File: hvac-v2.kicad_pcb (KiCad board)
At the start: 2 copper layers, 114 x 60 mm, 35 parts, among them J2 Anderson_two_redblack, J3 Anderson_two_redblack, J4 Anderson_two_redblack, P1 10118194, P2 CONN_01X08, SW1 SW_SPST, SW3 KS-01Q-01, SW4 KS-01Q-01, SW5 SPST, U1 SAMD21E18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

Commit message: Add silkscreen version and test/cal
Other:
- board text added: "CAL"
- board text added: "HVAC v2.0 By: CandyKingdom GDPR compliant"
- board text added: "TEST"
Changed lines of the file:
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@@
     (links 90)
     (no_connects 0)
-    (area 45.924999 44.924999 160.075001 104.075001)
+    (area 45.924999 43.924999 160.075001 104.075001)
     (thickness 1.6)
-    (drawings 4)
+    (drawings 59)
     (tracks 477)
     (zones 0)
@@
       (net 4 FAN_OUT))
   )
+  (gr_line (start 127.4 101.6) (end 127.8 101.6) (layer F.SilkS) (width 0.2))
+  (gr_line (start 127.8 101.6) (end 127.8 101.5) (layer F.SilkS) (width 0.2))
+  (gr_line (start 127.9 101.7) (end 127.9 101.4) (layer F.SilkS) (width 0.2))
+  (gr_line (start 127.9 101.4) (end 127.4 101.4) (layer F.SilkS) (width 0.2))
+  (gr_line (start 127.8 101.5) (end 127.5 101.5) (layer F.SilkS) (width 0.2))
+  (gr_line (start 127.4 101.4) (end 127.4 101.6) (layer F.SilkS) (width 0.2))
+  (gr_line (start 128 101.8) (end 128 101.3) (layer F.SilkS) (width 0.2))
+  (gr_line (start 127.2 101.7) (end 127.9 101.7) (layer F.SilkS) (width 0.2))
+  (gr_line (start 127.2 101.3) (end 127.2 101.7) (layer F.SilkS) (width 0.2))
+  (gr_line (start 127.1 101.2) (end 127.1 101.8) (layer F.SilkS) (width 0.2))
+  (gr_line (start 128 101.3) (end 127.2 101.3) (layer F.SilkS) (width 0.2))
+  (gr_line (start 128.1 101.2) (end 127.1 101.2) (layer F.SilkS) (width 0.2))
+  (gr_line (start 127.1 101.8) (end 128 101.8) (layer F.SilkS) (width 0.2))
+  (gr_line (start 128.4 100.8) (end 126.8 100.8) (layer F.SilkS) (width 0.2))
+  (gr_line (start 127 101.1) (end 127 101.9) (layer F.SilkS) (width 0.2))
+  (gr_line (start 126.9 101) (end 126.9 102) (layer F.SilkS) (width 0.2))
+  (gr_line (start 126.8 102.1) (end 128.4 102.1) (layer F.SilkS) (width 0.2))
+  (gr_line (start 126.8 100.8) (end 126.8 102.1) (layer F.SilkS) (width 0.2))
+  (gr_line (start 126.9 102) (end 128.2 102) (layer F.SilkS) (width 0.2))
+  (gr_line (start 128.2 102) (end 128.2 101.1) (layer F.SilkS) (width 0.2))
+  (gr_line (start 128.1 101.9) (end 128.1 101.2) (layer F.SilkS) (width 0.2))
+  (gr_line (start 127 101.9) (end 128.1 101.9) (layer F.SilkS) (width 0.2))
+  (gr_line (start 128.4 102.1) (end 128.4 101) (layer F.SilkS) (width 0.2))
+  (gr_line (start 128.4 100.8) (end 128.4 101) (layer F.SilkS) (width 0.2))
+  (gr_line (start 128.2 101.1) (end 127 101.1) (layer F.SilkS) (width 0.2))
+  (gr_line (start 128.4 101) (end 126.9 101) (layer F.SilkS) (width 0.2))
+  (gr_line (start 127.4 98.8) (end 127.4 99) (layer F.SilkS) (width 0.2))
+  (gr_line (start 127.2 98.7) (end 127.2 99.1) (layer F.SilkS) (width 0.2))
+  (gr_line (start 128 98.7) (end 127.2 98.7) (layer F.SilkS) (width 0.2))
+  (gr_line (start 128.1 98.6) (end 127.1 98.6) (layer F.SilkS) (width 0.2))
+  (gr_line (start 127.8 98.9) (end 127.5 98.9) (layer F.SilkS) (width 0.2))
+  (gr_line (start 127.8 99) (end 127.8 98.9) (layer F.SilkS) (width 0.2))
+  (gr_line (start 127.4 99) (end 127.8 99) (layer F.SilkS) (width 0.2))
+  (gr_line (start 127.9 98.8) (end 127.4 98.8) (layer F.SilkS) (width 0.2))
+  (gr_line (start 127.9 99.1) (end 127.9 98.8) (layer F.SilkS) (width 0.2))
+  (gr_line (start 127.2 99.1) (end 127.9 99.1) (layer F.SilkS) (width 0.2))
+  (gr_line (start 127.1 99.2) (end 128 99.2) (layer F.SilkS) (width 0.2))
+  (gr_line (start 127.1 98.6) (end 127.1 99.2) (layer F.SilkS) (width 0.2))
+  (gr_line (start 128 99.2) (end 128 98.7) (layer F.SilkS) (width 0.2))
+  (gr_line (start 128.1 99.3) (end 128.1 98.6) (layer F.SilkS) (width 0.2))
+  (gr_line (start 128.2 98.5) (end 127 98.5) (layer F.SilkS) (width 0.2))
+  (gr_line (start 127 99.3) (end 128.1 99.3) (layer F.SilkS) (width 0.2))
+  (gr_line (start 128.4 98.4) (end 126.9 98.4) (layer F.SilkS) (width 0.2))
+  (gr_line (start 126.9 99.4) (end 128.2 99.4) (layer F.SilkS) (width 0.2))
+  (gr_line (start 128.4 99.5) (end 128.4 98.4) (layer F.SilkS) (width 0.2))
+  (gr_line (start 128.4 98.2) (end 128.4 98.4) (layer F.SilkS) (width 0.2))
+  (gr_line (start 128.2 99.4) (end 128.2 98.5) (layer F.SilkS) (width 0.2))
+  (gr_line (start 127 98.5) (end 127 99.3) (layer F.SilkS) (width 0.2))
+  (gr_line (start 126.9 98.4) (end 126.9 99.4) (layer F.SilkS) (width 0.2))
+  (gr_line (start 126.8 99.5) (end 128.4 99.5) (layer F.SilkS) (width 0.2))
+  (gr_line (start 126.8 98.2) (end 126.8 99.5) (layer F.SilkS) (width 0.2))
+  (gr_line (start 128.4 98.2) (end 126.8 98.2) (layer F.SilkS) (width 0.2))
+  (gr_text CAL (at 131 98.9) (layer F.SilkS)
+    (effects (font (size 1.5 1.5) (thickness 0.3)))
+  )
+  (gr_text TEST (at 131.6 101.5) (layer F.SilkS)
+    (effects (font (size 1.5 1.5) (thickness 0.3)))
+  )
+  (gr_text "HVAC v2.0\nBy: CandyKingdom\nGDPR compliant" (at 107.7 95.2) (layer F.SilkS)
+    (effects (font (size 1.5 1.5) (thickness 0.3)))
+  )
   (gr_line (start 46 104) (end 46 44) (layer Edge.Cuts) (width 0.15))

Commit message: Place the programming header and diode
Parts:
- added D1: BAT54GWJ, Diodes_SMD:SOD-123, F.Cu at (60.3, 83.6)
- added J1: Conn_01x04, Pin_Headers:Pin_Header_Straight_1x04, F.Cu at (112.1, 101.8)
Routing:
- net ARM_SWCLK: track 0.00 -> 27.2 mm, vias 0 -> 2
- net ARM_SWDIO: track 0.00 -> 24.9 mm, vias 0 -> 2
- net VCC: track 391.0 -> 405.2 mm, vias 15 -> 16
- net Net-(D1-Pad2): track 0.00 -> 10.2 mm
- net +BATT: track 183.2 -> 190.2 mm
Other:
- board text added: "FAN"
- board text added: "GND CLK IO VCC"
- board text added: "IN"
- board text added: "PUMP"

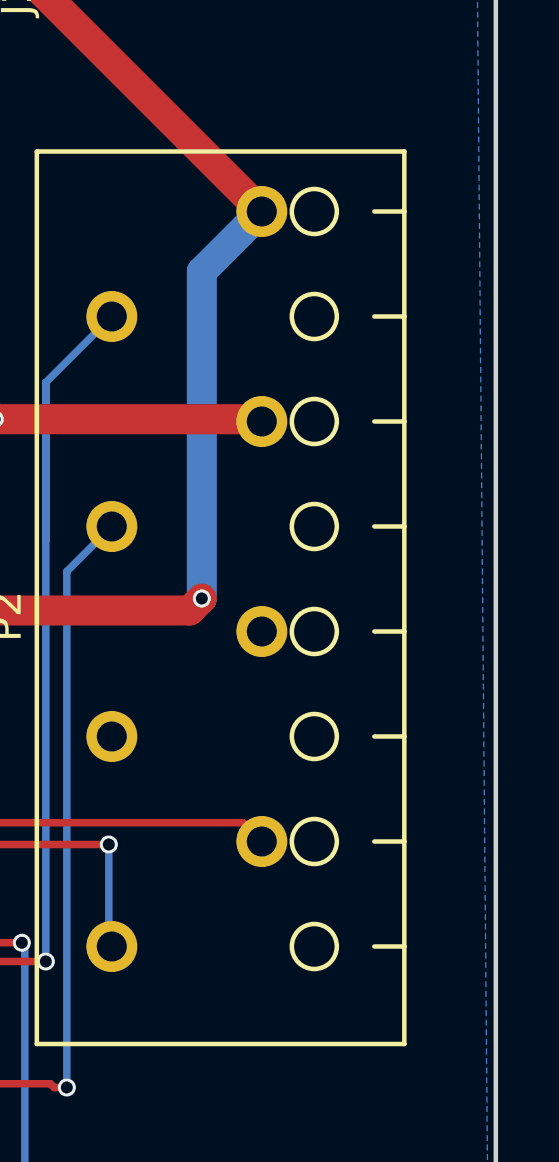
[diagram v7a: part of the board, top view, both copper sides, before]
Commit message: More silkscreens + generate assembly sheet
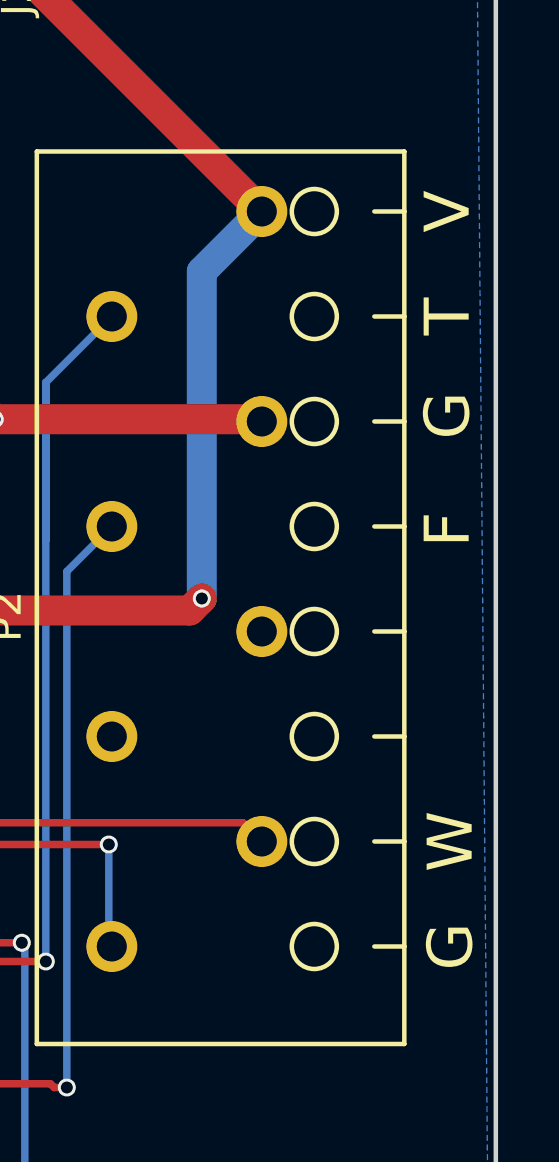
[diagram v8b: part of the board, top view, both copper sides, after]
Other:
- board text added: "BIG DIODE"
- board text added: "BUTTON"
- board text added: "CPU"
- board text added: "F"
- board text added: "FUSE"
- board text added: "G"
- board text added: "LED"
- board text added: "MOSFET"
- board text added: "POWER_SW"
- board text added: "T"
- board text added: "TEMP PROBE"
- board text added: "TINY DIODE"
- board text added: "V"
- board text added: "V: VCC T: EXTERNAL TEMP G: GROUND F: FAN W: WATER SWITCH"
- board text added: "W"
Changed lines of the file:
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@@
     (links 96)
     (no_connects 0)
-    (area 44.036499 35.224999 160.075001 106.622619)
+    (area 45.924999 43.924999 160.075001 104.075001)
     (thickness 1.6)
-    (drawings 67)
+    (drawings 89)
     (tracks 501)
     (zones 0)
@@
   (page A4)
   (layers
-    (0 F.Cu signal)
-    (31 B.Cu signal)
-    (32 B.Adhes user)
-    (33 F.Adhes user)
-    (34 B.Paste user)
-    (35 F.Paste user)
-    (36 B.SilkS user)
+    (0 F.Cu signal hide)
+    (31 B.Cu signal hide)
+    (32 B.Adhes user hide)
+    (33 F.Adhes user hide)
+    (34 B.Paste user hide)
+    (35 F.Paste user hide)
+    (36 B.SilkS user hide)
     (37 F.SilkS user)
     (38 B.Mask user)
@@
       (effects (font (size 1 1) (thickness 0.15)))
     )
-    (fp_text value Anderson_two_redblack (at -9.25 -14.5 90) (layer F.Fab)
+    (fp_text value Anderson_two_redblack (at -0.16 -14.7 90) (layer F.Fab)
       (effects (font (size 1 1) (thickness 0.15)))
     )
@@
       (effects (font (size 1 1) (thickness 0.15)))
     )
-    (fp_text value POT (at 0 -18) (layer F.Fab)
+    (fp_text value POT (at 0.1 -9.5) (layer F.Fab)
       (effects (font (size 1 1) (thickness 0.15)))
     )
@@
       (effects (font (size 1 1) (thickness 0.15)))
     )
-    (fp_text value Anderson_two_redblack (at -9.25 -14.5 90) (layer F.Fab)
+    (fp_text value Anderson_two_redblack (at -0.24 -15.3 90) (layer F.Fab)
       (effects (font (size 1 1) (thickness 0.15)))
     )
@@
       (effects (font (size 1 1) (thickness 0.15)))
     )
-    (fp_text value 10uF (at 0 2.1 90) (layer F.Fab)
+    (fp_text value 10uF (at 4.1 -0.1 90) (layer F.Fab)
       (effects (font (size 1 1) (thickness 0.15)))
     )
@@
       (effects (font (size 1 1) (thickness 0.15)))
     )
-    (fp_text value 1uF (at 0 1.9 90) (layer F.Fab)
+    (fp_text value 1uF (at 3.15 0.1 90) (layer F.Fab)
       (effects (font (size 1 1) (thickness 0.15)))
     )
@@
       (effects (font (size 1 1) (thickness 0.15)))
     )
-    (fp_text value 1uF (at 0 1.9 90) (layer F.Fab)
+    (fp_text value 1uF (at 3.15 0.1 90) (layer F.Fab)
       (effects (font (size 1 1) (thickness 0.15)))
     )
@@
       (effects (font (size 1 1) (thickness 0.15)))
     )
-    (fp_text value BK-6010 (at 0 -10.75 180) (layer F.Fab)
+    (fp_text value BK-6010 (at -0.1 -0.3 180) (layer F.Fab)
       (effects (font (size 1 1) (thickness 0.15)))
     )
@@
       (effects (font (size 1 1) (thickness 0.15)))
     )
-    (fp_text value Anderson_two_redblack (at -9.25 -14.5 90) (layer F.Fab)
+    (fp_text value Anderson_two_redblack (at -0.19 -14.6 90) (layer F.Fab)
       (effects (font (size 1 1) (thickness 0.15)))
     )
@@
       (effects (font (size 1 1) (thickness 0.15)))
     )
-    (fp_text value 470 (at 0 1.9 180) (layer F.Fab)
+    (fp_text value 470 (at 0.1 -2 180) (layer F.Fab)
       (effects (font (size 1 1) (thickness 0.15)))
     )
@@
       (effects (font (size 1 1) (thickness 0.15)))
     )
-    (fp_text value 470 (at 0 1.9 270) (layer F.Fab)
+    (fp_text value 470 (at 0 -1.9 270) (layer F.Fab)
       (effects (font (size 1 1) (thickness 0.15)))
     )
@@
       (effects (font (size 1 1) (thickness 0.15)))
     )
-    (fp_text value POT (at 0 -18) (layer F.Fab)
+    (fp_text value POT (at 0.1 -9.4) (layer F.Fab)
       (effects (font (size 1 1) (thickness 0.15)))
     )
@@
       (effects (font (size 1 1) (thickness 0.15)))
     )
-    (fp_text value Conn_01x04 (at 0 -3.1 270) (layer F.Fab)
+    (fp_text value Conn_01x04 (at -2.9 3.4 360) (layer F.Fab) hide
       (effects (font (size 1 1) (thickness 0.15)))
     )
@@
       (effects (font (size 1 1) (thickness 0.15)))
     )
-    (fp_text value BAT54GWJ (at 0 2.1 270) (layer F.Fab)
+    (fp_text value BAT54GWJ (at 0 2.1 270) (layer F.Fab) hide
       (effects (font (size 1 1) (thickness 0.15)))
     )
@@
       (net 8 "Net-(D1-Pad2)"))
   )
+  (gr_text CPU (at 124.1 81.7) (layer F.Fab)
+    (effects (font (size 1.5 1.5) (thickness 0.3)))
+  )
+  (gr_text "TINY DIODE" (at 61.2 83.8 360) (layer F.Fab)
+    (effects (font (size 1.5 1.5) (thickness 0.3)))
+  )
+  (gr_text BUTTON (at 107.6 75.6) (layer F.Fab)
+    (effects (font (size 1.5 1.5) (thickness 0.3)))
+  )
+  (gr_text "BIG DIODE" (at 86.8 78.3) (layer F.Fab)
+    (effects (font (size 1.5 1.5) (thickness 0.3)))
+  )
+  (gr_text MOSFET (at 71.6 71.2) (layer F.Fab)
+    (effects (font (size 1.5 1.5) (thickness 0.3)))
+  )
+  (gr_text MOSFET (at 95.1 61.8) (layer F.Fab)
+    (effects (font (size 1.5 1.5) (thickness 0.3)))
+  )
+  (gr_text FUSE (at 106.1 46.9) (layer F.Fab)
+    (effects (font (size 1.5 1.5) (thickness 0.3)))
+  )
+  (gr_text POWER_SW (at 118.4 55.5 90) (layer F.Fab)
+    (effects (font (size 1.5 1.5) (thickness 0.3)))
+  )
+  (gr_text BUTTON (at 87.5 90.5) (layer F.Fab)
+    (effects (font (size 1.5 1.5) (thickness 0.3)))
+  )
+  (gr_text BUTTON (at 50.4 73.2) (layer F.Fab)
+    (effects (font (size 1.5 1.5) (thickness 0.3)))
+  )
+  (gr_text "BIG DIODE" (at 63.8 78.1) (layer F.Fab)
+    (effects (font (size 1.5 1.5) (thickness 0.3)))
+  )
+  (gr_text LED (at 122.3 66.3) (layer F.Fab)
+    (effects (font (size 1.5 1.5) (thickness 0.3)))
+  )
+  (gr_text LED (at 87.2 84.8) (layer F.Fab)
+    (effects (font (size 1.5 1.5) (thickness 0.3)))
+  )
+  (gr_text LED (at 53.9 60.8) (layer F.Fab)
+    (effects (font (size 1.5 1.5) (thickness 0.3)))
+  )
+  (gr_text W (at 158.5 83.9 90) (layer F.SilkS)
+    (effects (font (size 1.5 1.5) (thickness 0.3)))
+  )
+  (gr_text G (at 158.5 87.4 90) (layer F.SilkS)
+    (effects (font (size 1.5 1.5) (thickness 0.3)))
+  )
+  (gr_text F (at 158.4 73.5 90) (layer F.SilkS)
+    (effects (font (size 1.5 1.5) (thickness 0.3)))
+  )
+  (gr_text G (at 158.4 69.7 90) (layer F.SilkS)
+    (effects (font (size 1.5 1.5) (thickness 0.3)))
+  )
+  (gr_text T (at 158.4 66.4 90) (layer F.SilkS)
+    (effects (font (size 1.5 1.5) (thickness 0.3)))
+  )
+  (gr_text V (at 158.4 62.9 90) (layer F.SilkS)
+    (effects (font (size 1.5 1.5) (thickness 0.3)))
+  )
+  (gr_text "V: VCC\nT: EXTERNAL TEMP\nG: GROUND\nF: FAN\nW: WATER SWITCH" (at 151.8 65.7 90) (layer B.SilkS)
+    (effects (font (size 1.5 1.5) (thickness 0.3)) (justify left mirror))
+  )
+  (gr_text "TEMP PROBE" (at 140.2 97.7) (layer F.Fab)
+    (effects (font (size 1.5 1.5) (thickness 0.3)))
+  )
   (gr_text FAN (at 56 46.1 180) (layer F.SilkS)
